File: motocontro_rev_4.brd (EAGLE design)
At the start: 160 x 100 mm, 27 parts

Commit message: Finished schematic, board almost done
Board layout in progress
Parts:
- removed CURR_RES: 40 mOhm, eagle-ltspice:R6332
- removed U$4: TRACO-TSR-1-2450, r-78xx_10:SIP3
- removed U$5: FERD40H100SG-TR, motocontro_rev_4:TO-263/D2PAK
- added LDO: TRACO-TSR-1-2450, r-78xx_10:SIP3
- added RSENSE1: 37m, motocontro_rev_4:2818_WITH_VIA
- added SCHOTTKY: FERD40H100SG-TR, motocontro_rev_4:TO-263/D2PAK
- CURR_RES1: value 40 mOhm -> 37m; device eagle-ltspice:R6332 -> motocontro_rev_4:2818_WITH_VIA
- moved C3 341.2 mm to (137.6, 62.9)
- moved C1 339.6 mm to (139.4, 50.5)
- moved C2 337.8 mm to (144.8, 35.8)
- moved R7 328.3 mm to (71.3, 43.7), turned to 90 degrees
- moved R6 324.2 mm to (74.7, 43.6), turned to 270 degrees
- moved R5 313.1 mm to (72.7, 38.4)
- moved R3 250.2 mm to (85.5, 59.4), turned to 180 degrees
- moved R4 249.1 mm to (85.5, 51.8), turned to 180 degrees
- moved CSD 228.6 mm to (57.3, 55.5), turned to 90 degrees
- moved RSD 227.7 mm to (57.3, 60.9), turned to 90 degrees
- moved U$3 220.5 mm to (24.4, 23.5), turned to 90 degrees
- moved CDT1 211.7 mm to (66.6, 43.5), turned to 90 degrees
- moved R2 198.7 mm to (62.1, 43.3), turned to 90 degrees
- moved CDT 195.5 mm to (56.7, 49.7), turned to 90 degrees
- moved RDT 193.7 mm to (61.6, 49.5), turned to 90 degrees
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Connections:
- removed net #SD/OD: CSD.2, RSD.1, U$1.2
- new net SD/OD: CSD.2, RSD.1, U$1.2, U$2.5
- net 5V: now also LDO.3; no longer U$4.3
- net DGND: now also LDO.2; no longer U$4.2
- net GND: now also U$3.ON/OFF
- net OPOUT: now also U$2.14/A0
- net OUT: now also SCHOTTKY.3; no longer U$5.3
- net PGND: now also CURR_RES1.P$1, CURR_RES1.P1.1, RSENSE1.P$1, RSENSE1.P1.1; no longer CURR_RES.1, CURR_RES1.1
- net PWM: now also U$2.6
- net RSENSE+: now also CURR_RES1.P$2, CURR_RES1.P2.2, RSENSE1.P$2, RSENSE1.P2.2; no longer CURR_RES.2, CURR_RES1.2
- net VBUS: now also SCHOTTKY.2; no longer U$5.2
- net VCC: now also LDO.1; no longer U$4.1
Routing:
- net OUT: track 0.00 -> 47.3 mm
- net OPOUT: track 0.00 -> 44.5 mm
- net SD/OD: track 0.00 -> 42.9 mm, vias 0 -> 2
- net PWM: track 0.00 -> 39.7 mm, vias 0 -> 1
- net OP+: track 0.00 -> 22.4 mm
- net PGND: track 0.00 -> 19.3 mm
- net DGND: track 0.00 -> 15.0 mm, vias 0 -> 5
- net OP-: track 0.00 -> 13.3 mm
- net 5V: track 0.00 -> 12.2 mm
- net DT: track 0.00 -> 12.1 mm
- net HVG: track 0.00 -> 9.51 mm
- net LVG: track 0.00 -> 9.29 mm
- net RSENSE+: track 0.00 -> 8.68 mm
- net N$3: track 0.00 -> 7.01 mm
- net N$2: track 0.00 -> 5.49 mm
- added copper zone on layer 16, net DGND
- added copper zone on layer 1, net OUT
- added copper zone on layer 1, net PGND
- added copper zone on layer 1, net RSENSE+
- added copper zone on layer 1, net VBUS
- added copper zone on layer 16, net VBUS
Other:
- board size 160 x 100 mm -> 160 x 89 mm
- board text added: "REV Half-Bridge Motor Controller"

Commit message: redos some layout
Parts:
- C1: value 22u -> 1u; device adafruit:175TMP-0810 -> Nordic_nRF:RESC0805_M
- moved C2 148.7 mm to (2.81, -8.19)
- moved C3 132.7 mm to (23.6, -5.06)
- moved SCHOTTKY 94.6 mm to (209.4, 50.1), turned to 270 degrees
- moved C1 80.1 mm to (59.4, 53.5), turned to 270 degrees
- moved CURR_RES1 44.4 mm to (74.4, -9.91)
- moved RSENSE1 43.5 mm to (65.1, -8.69)
- moved BATTERY 31.8 mm to (102.5, -1.92)
- moved MOTOR 31.8 mm to (141.1, -1.92)
- moved LDO 24.1 mm to (56.0, 27.2), turned to 270 degrees
- moved CBOOT 14.2 mm to (80.1, 66.2), turned to 270 degrees
- moved R5 10.9 mm to (81.8, 44.3)
- moved R1 9.21 mm to (65.6, 47.1), turned to 180 degrees
- moved HS_FET 9.00 mm to (98.1, 71.9), turned to 270 degrees
- moved R7 7.71 mm to (78.8, 41.9)
- moved RDT 7.21 mm to (55.6, 53.5)
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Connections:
- net DGND: now also C1.2; no longer C1.-
- net VCC: now also C1.1; no longer C1.+
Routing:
- net OUT: track 47.3 -> 0.00 mm
- net PWM: track 39.7 -> 0.00 mm, vias 1 -> 0
- net SD/OD: track 42.9 -> 15.1 mm, vias 2 -> 0
- net OPOUT: track 44.5 -> 17.1 mm, vias 0 -> 2
- net OP+: track 22.4 -> 0.00 mm
- net PGND: track 19.3 -> 0.00 mm
- net 5V: track 12.2 -> 0.00 mm
- net HVG: track 9.51 -> 0.00 mm
- net LVG: track 9.29 -> 0.00 mm
- net RSENSE+: track 8.68 -> 0.00 mm
- net N$3: track 7.01 -> 0.00 mm
- net N$2: track 5.49 -> 0.00 mm
- net DT: track 12.1 -> 16.6 mm
- net OP-: track 13.3 -> 16.8 mm, vias 0 -> 2
- net DGND: vias 5 -> 0
- added copper zone on layer 1, net VCC
- removed copper zone on layer 1, net OUT
- removed copper zone on layer 1, net PGND
- removed copper zone on layer 1, net RSENSE+
- removed copper zone on layer 1, net VBUS
- removed copper zone on layer 16, net VBUS

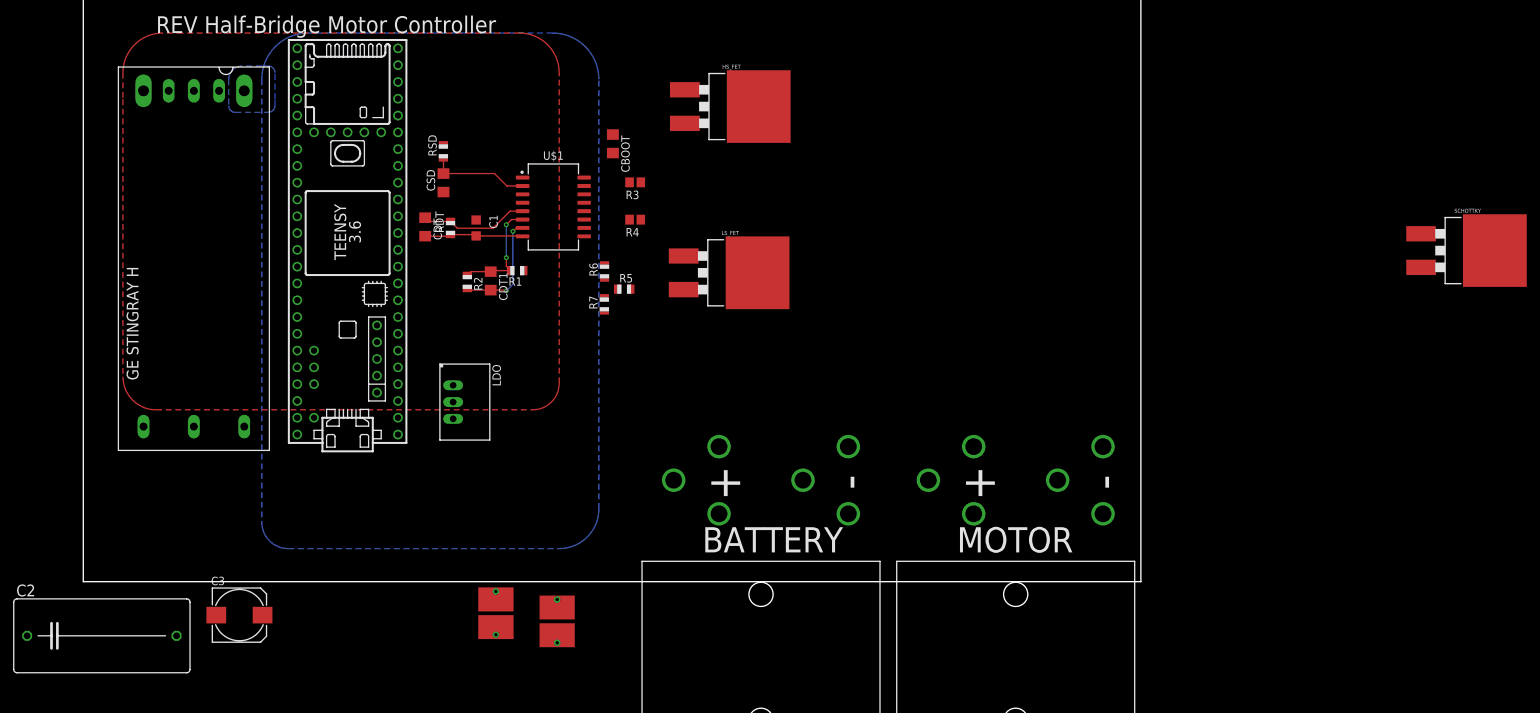
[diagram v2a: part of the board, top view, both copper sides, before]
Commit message: finishes layout
finishes layout and minimal changes to teensy pinout.
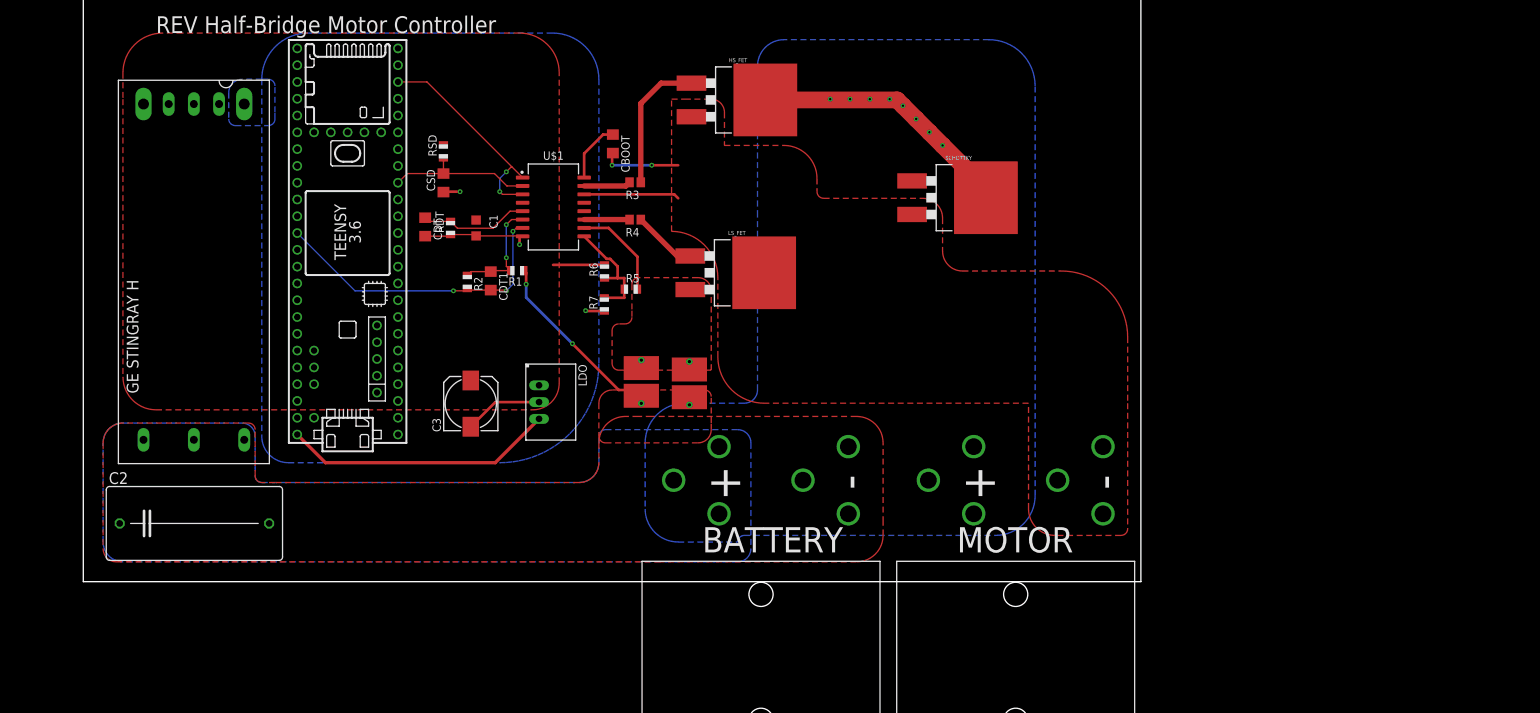
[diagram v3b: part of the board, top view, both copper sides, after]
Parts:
- moved SCHOTTKY 77.4 mm to (132.4, 58.1)
- moved C3 47.4 mm to (58.6, 26.9), turned to 90 degrees
- moved RSENSE1 41.3 mm to (87.1, 26.3)
- moved CURR_RES1 41.2 mm to (94.4, 26.1)
- moved C2 22.0 mm to (16.8, 8.81)
- moved LDO 13.0 mm to (69.0, 27.2)
- moved U$3 2.00 mm to (24.4, 21.5)
- moved HS_FET 1.41 mm to (99.1, 72.9)
- moved LS_FET 1.00 mm to (98.9, 46.7)
- moved R5 1.00 mm to (82.8, 44.3)
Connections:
- removed net GND: C2.2, U$3.ON/OFF, U$3.VI-
- net PGND: now also C2.2, U$3.ON/OFF, U$3.VI-
- net PWM: now also U$2.30; no longer U$2.6
- net SD/OD: now also U$2.24; no longer U$2.5
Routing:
- net VBUS: track 0.00 -> 42.5 mm, vias 0 -> 8
- net 5V: track 0.00 -> 41.1 mm
- net PWM: track 0.00 -> 33.0 mm, vias 0 -> 2
- net OPOUT: track 17.1 -> 46.6 mm, vias 2 -> 3
- net OUT: track 0.00 -> 26.4 mm, vias 0 -> 2
- net PGND: track 0.00 -> 26.0 mm, vias 0 -> 2
- net N$2: track 0.00 -> 20.9 mm
- net DGND: track 15.0 -> 34.0 mm, vias 0 -> 3
- net OP+: track 0.00 -> 17.7 mm
- net RSENSE+: track 0.00 -> 14.8 mm
- net N$3: track 0.00 -> 9.77 mm
- net VBOOT: track 0.00 -> 9.17 mm
- net VCC: track 0.00 -> 7.78 mm
- net SD/OD: track 15.1 -> 22.6 mm
- net HVG: track 0.00 -> 7.10 mm
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- added copper zone on layer 1, net OUT
- added copper zone on layer 1, net PGND
- added copper zone on layer 1, net RSENSE+
- added copper zone on layer 16, net VBUS

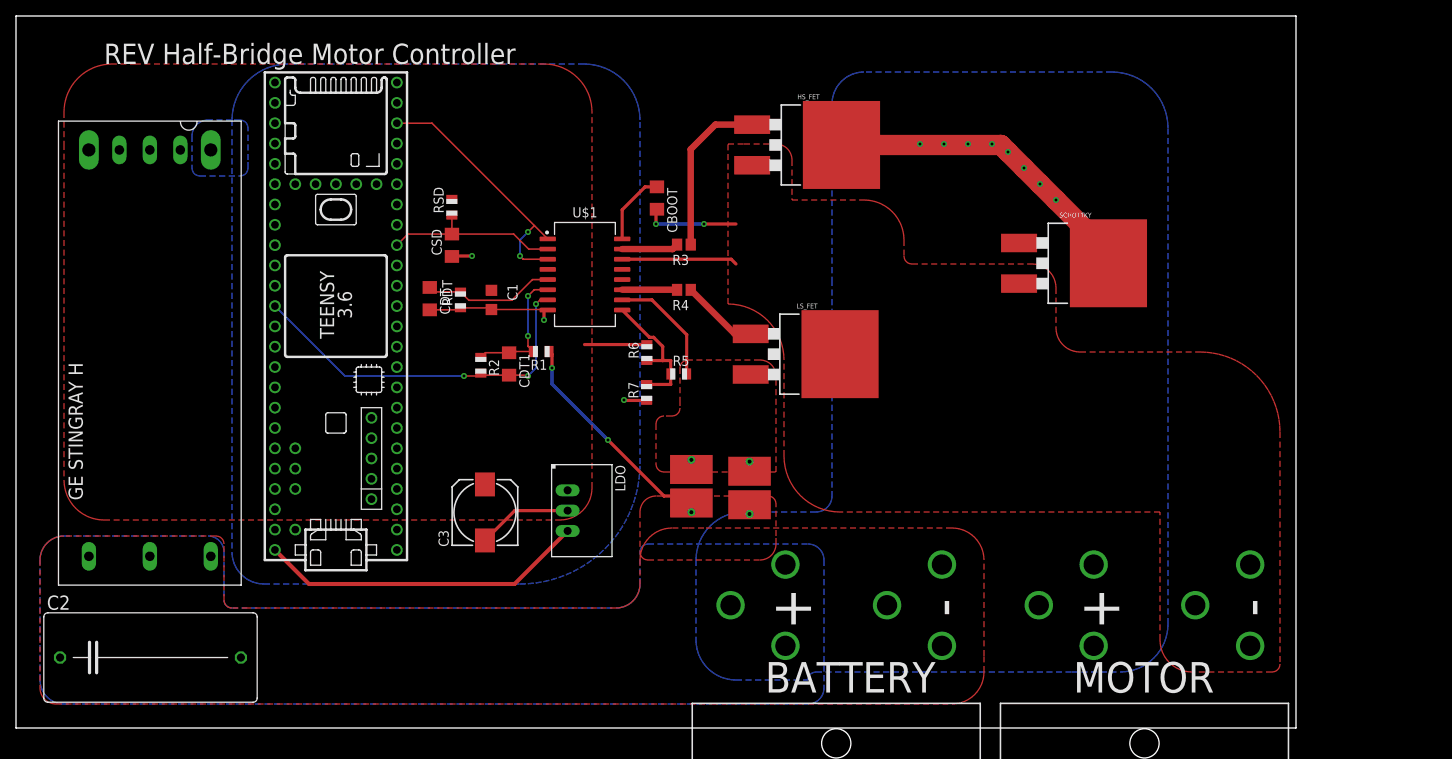
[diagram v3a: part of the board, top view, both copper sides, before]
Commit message: Design Review
Added a ton of notes of things to be updated
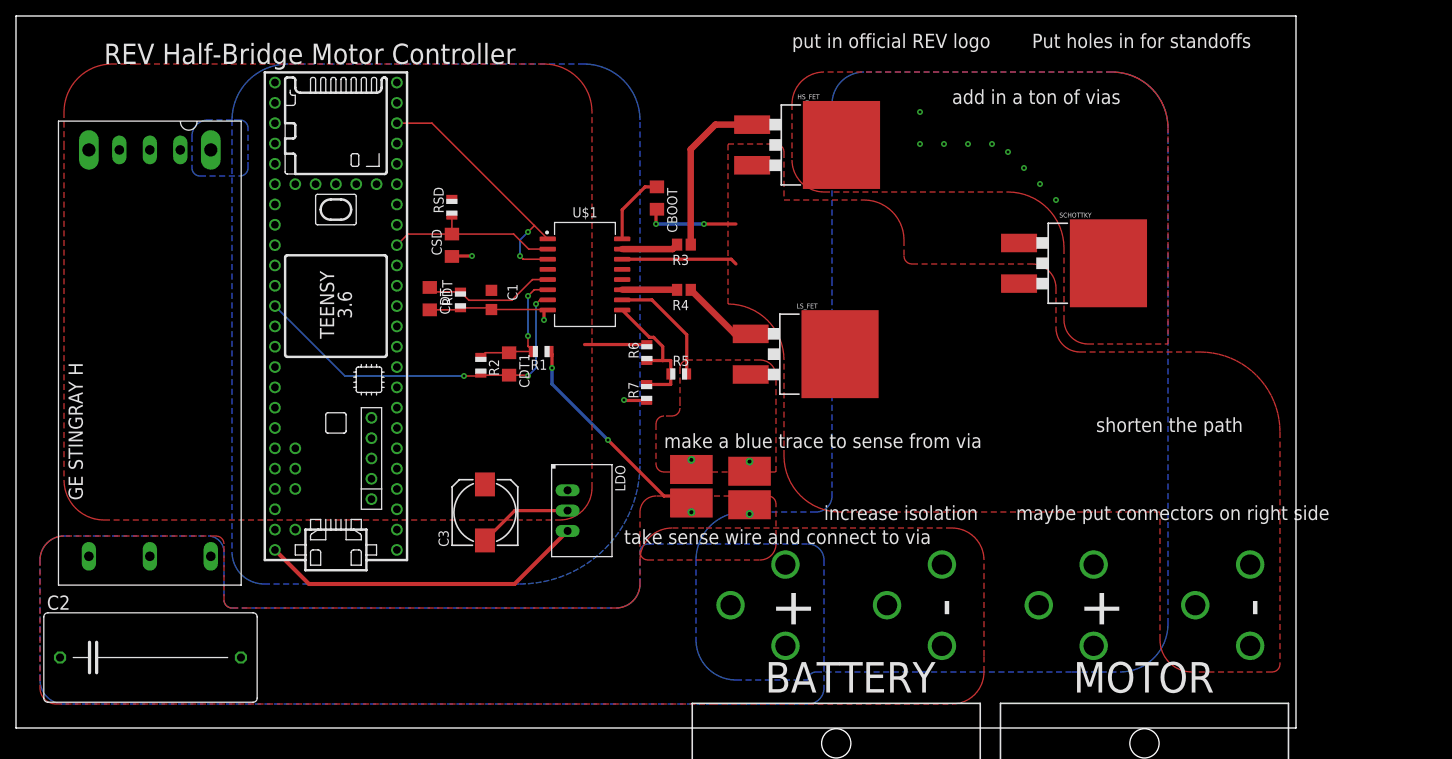
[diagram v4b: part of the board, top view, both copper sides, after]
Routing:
- net VBUS: track 42.5 -> 1.48 mm, vias 8 -> 9
- added copper zone on layer 1, net VBUS
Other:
- board text added: "Put holes in for standoffs"
- board text added: "add in a ton of vias"
- board text added: "increase isolation"
- board text added: "make a blue trace to sense from via"
- board text added: "maybe put connectors on right side"
- board text added: "put in official REV logo"
- board text added: "shorten the path"
- board text added: "take sense wire and connect to via"
